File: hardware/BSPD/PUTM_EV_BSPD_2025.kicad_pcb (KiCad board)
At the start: 2 copper layers, 0 parts

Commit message: Layout and connections added
First version of board layout and connections added, to be checked and improved 

I know about 4 DRC errors, I will fix them, but that is what i have for now
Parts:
- added C1: 1u, Capacitor_SMD:C_0805_2012Metric, B.Cu at (137.8, 102.7)
- added C10: 100n, Capacitor_SMD:C_0603_1608Metric, F.Cu at (149.5, 104.2)
- added C11: 100n, Capacitor_SMD:C_0603_1608Metric, F.Cu at (137.7, 93.5)
- added C12: 100n, Capacitor_SMD:C_0603_1608Metric, F.Cu at (149.1, 107.6)
- added C13: 100n, Capacitor_SMD:C_0603_1608Metric, F.Cu at (131.8, 106.6)
- added C14: 100n, Capacitor_SMD:C_0603_1608Metric, B.Cu at (142.7, 103.6)
- added C15: 100n, Capacitor_SMD:C_0603_1608Metric, F.Cu at (139.0, 99.8)
- added C16: 100n, Capacitor_SMD:C_0603_1608Metric, F.Cu at (138.1, 97.4)
- added C17: 100n, Capacitor_SMD:C_0603_1608Metric, F.Cu at (144.9, 97.0)
- added C19: 100n, Capacitor_SMD:C_0603_1608Metric, F.Cu at (147.5, 91.2)
- added C2: 1u, Capacitor_SMD:C_0805_2012Metric, B.Cu at (137.8, 105.7)
- added C20: 100n, Capacitor_SMD:C_0603_1608Metric, F.Cu at (157.4, 99.2)
- added C3: 100nF, Capacitor_SMD:C_0603_1608Metric, B.Cu at (125.9, 94.3)
- added C4: 1u, Capacitor_SMD:C_0805_2012Metric, B.Cu at (137.8, 108.7)
- added C5: 100nF, Capacitor_SMD:C_0603_1608Metric, B.Cu at (125.9, 96.8)
- added C6: 1u, Capacitor_SMD:C_0805_2012Metric, B.Cu at (137.8, 111.7)
- added C7: 1u, Capacitor_SMD:C_0603_1608Metric, F.Cu at (154.7, 92.0)
- added C8: 10n, Capacitor_SMD:C_0603_1608Metric, B.Cu at (147.7, 103.6)
- added C9: 1u, Capacitor_SMD:C_0603_1608Metric, B.Cu at (146.0, 103.6)
- added D1: SK36A-LTP, Diode_SMD:D_SMA, B.Cu at (154.3, 114.4)
- added D2: D5V0L1B2T-7, Diode_SMD:D_SOD-523, F.Cu at (126.3, 107.0)
- added D3: LBD52A24L01, Diode_SMD:D_SOD-523, B.Cu at (126.1, 99.2)
- added D4: D5V0L1B2T-7, Diode_SMD:D_SOD-523, F.Cu at (141.9, 107.6)
- added D5: NSVRB751V40T1G, Diode_SMD:D_SOD-323_HandSoldering, B.Cu at (150.2, 98.6)
- added D8: D5V0L1B2T-7, Diode_SMD:D_SOD-523, F.Cu at (131.7, 103.4)
- added F1: 500mA, Capacitor_SMD:C_1812_4532Metric, B.Cu at (132.1, 112.0)
- added J1: BS1, Connector_Wire:SolderWire-0.1sqmm_1x02_P3.6mm_D0.4mm_OD1mm_Relief, F.Cu at (116.1, 116.0)
- added J2: BS2, Connector_Wire:SolderWire-0.1sqmm_1x02_P3.6mm_D0.4mm_OD1mm_Relief, F.Cu at (116.1, 109.0)
- added J3: BS2, Connector_Wire:SolderWire-0.1sqmm_1x02_P3.6mm_D0.4mm_OD1mm_Relief, F.Cu at (116.1, 102.0)
- added J4: Conn_01x02, Connector_Wire:SolderWire-0.1sqmm_1x02_P3.6mm_D0.4mm_OD1mm_Relief, F.Cu at (116.1, 95.0)
- added JP1: Solder bridge, Jumper:SolderJumper-2_P1.3mm_Open_RoundedPad1.0x1.5mm, F.Cu at (168.1, 107.6)
- added JP2: Solder bridge, Jumper:SolderJumper-2_P1.3mm_Open_RoundedPad1.0x1.5mm, F.Cu at (168.1, 111.4)
- added K2: TE AXICOM IM07DTS, footprints:IM23TS, F.Cu at (162.1, 111.5)
- added Q1: BS170F, Package_TO_SOT_SMD:SOT-23, B.Cu at (159.1, 104.0)
- added R1: 10k, Resistor_SMD:R_0603_1608Metric_Pad0.98x0.95mm_HandSolder, F.Cu at (127.7, 97.2)
- added R10: 10k, Resistor_SMD:R_0603_1608Metric, F.Cu at (148.0, 114.9)
- added R11: 1k, Resistor_SMD:R_0603_1608Metric, F.Cu at (134.4, 107.4)
- added R12: 1k, Resistor_SMD:R_0603_1608Metric, F.Cu at (148.0, 113.2)
- added R13: 10k, Resistor_SMD:R_0603_1608Metric, F.Cu at (136.5, 109.1)
- added R14: 10k, Resistor_SMD:R_0603_1608Metric, F.Cu at (141.9, 110.8)
- added R15: 10k, Resistor_SMD:R_0603_1608Metric, F.Cu at (152.8, 110.0)
- added R18: 50k, Resistor_SMD:R_0603_1608Metric, F.Cu at (154.7, 90.3)
- added R19: 100k, Resistor_SMD:R_0603_1608Metric, F.Cu at (154.7, 93.7)
- added R2: 10k, Resistor_SMD:R_0603_1608Metric_Pad0.98x0.95mm_HandSolder, F.Cu at (127.7, 99.0)
- added R20: 10k, Resistor_SMD:R_0603_1608Metric, F.Cu at (155.7, 104.8)
- added R22: 1k, Resistor_SMD:R_0603_1608Metric, F.Cu at (156.2, 95.5)
- added R23: 1k, Resistor_SMD:R_0603_1608Metric, F.Cu at (156.1, 97.3)
- added R3: 1k, Resistor_SMD:R_0603_1608Metric_Pad0.98x0.95mm_HandSolder, F.Cu at (132.1, 100.2)
- added R4: 10k, Resistor_SMD:R_0603_1608Metric, F.Cu at (158.9, 90.2)
- added R5: 4k, Resistor_SMD:R_0603_1608Metric_Pad0.98x0.95mm_HandSolder, F.Cu at (132.1, 101.8)
- added R6: 10M, Resistor_SMD:R_0603_1608Metric, B.Cu at (144.3, 103.6)
- added R7: 10k, Resistor_SMD:R_0603_1608Metric_Pad0.98x0.95mm_HandSolder, F.Cu at (139.5, 93.3)
- added R8: 10k, Resistor_SMD:R_0603_1608Metric, F.Cu at (126.3, 110.0)
- added R9: 10k, Resistor_SMD:R_0603_1608Metric, F.Cu at (134.4, 105.6)
- added RV1: 20k, Potentiometer_THT:Potentiometer_Bourns_3296W_Vertical, F.Cu at (133.1, 115.1)
- added RV2: 20k, Potentiometer_THT:Potentiometer_Bourns_3296W_Vertical, F.Cu at (143.6, 115.1)
- added RV3: 20k, Potentiometer_THT:Potentiometer_Bourns_3296W_Vertical, F.Cu at (133.7, 92.2)
- added SDC: SDC, Connector_Wire:SolderWire-0.1sqmm_1x02_P3.6mm_D0.4mm_OD1mm_Relief, F.Cu at (169.7, 99.7)
- added TP1: TestPoint, TestPoint:TestPoint_Pad_D1.0mm, B.Cu at (119.3, 112.4)
- added TP10: TestPoint, TestPoint:TestPoint_Pad_D1.0mm, F.Cu at (167.4, 91.6)
- added TP11: TestPoint, TestPoint:TestPoint_Pad_D1.0mm, B.Cu at (145.7, 91.4)
- added TP12: TestPoint, TestPoint:TestPoint_Pad_D1.0mm, F.Cu at (152.8, 104.9)
- added TP13: TestPoint, TestPoint:TestPoint_Pad_D1.0mm, F.Cu at (160.3, 97.3)
- added TP2: TestPoint, TestPoint:TestPoint_Pad_D1.0mm, B.Cu at (119.3, 105.4)
- added TP3: TestPoint, TestPoint:TestPoint_Pad_D1.0mm, B.Cu at (150.2, 91.7)
- added TP4: TestPoint, TestPoint:TestPoint_Pad_D1.0mm, F.Cu at (142.4, 105.0)
- added TP5: TestPoint, TestPoint:TestPoint_Pad_D1.0mm, F.Cu at (145.6, 99.6)
- added TP6: TestPoint, TestPoint:TestPoint_Pad_D1.0mm, F.Cu at (126.6, 102.0)
- added TP7: TestPoint, TestPoint:TestPoint_Pad_D1.0mm, F.Cu at (137.7, 90.6)
- added TP8: TestPoint, TestPoint:TestPoint_Pad_D1.0mm, B.Cu at (119.4, 98.4)
- added TP9: TestPoint, TestPoint:TestPoint_Pad_D1.0mm, B.Cu at (151.0, 94.0)
- added U1: MC78M12CDTG, Package_TO_SOT_SMD:TO-252-3_TabPin2, B.Cu at (133.1, 97.2)
- added U10: LM393B, Package_SO:TSSOP-8_3x3mm_P0.65mm, F.Cu at (160.4, 92.8)
- added U12: 74AHC1G08, Package_TO_SOT_SMD:SC-74A-5_1.55x2.9mm_P0.95mm, F.Cu at (149.1, 96.0)
- added U13: LM393B, Package_SO:TSSOP-8_3x3mm_P0.65mm, F.Cu at (133.2, 97.0)
- added U2: LM1117IMP-5.0, Package_TO_SOT_SMD:SOT-223-3_TabPin2, B.Cu at (130.7, 105.4)
- added U3: 74HC2G14-Q100, Package_SO:TSOP-6_1.65x3.05mm_P0.95mm, F.Cu at (145.0, 91.3)
- added U4: LM393B, Package_SO:TSSOP-8_3x3mm_P0.65mm, F.Cu at (131.2, 110.3)
- added U5: 74AHC1G08, Package_TO_SOT_SMD:SC-74A-5_1.55x2.9mm_P0.95mm, F.Cu at (154.8, 101.8)
- added U6: 74HC2G14-Q100, Package_SO:TSOP-6_1.65x3.05mm_P0.95mm, F.Cu at (139.2, 102.3)
- added U7: LM393B, Package_SO:TSSOP-8_3x3mm_P0.65mm, F.Cu at (147.8, 110.3)
- added U8: NE555DR, Package_SO:SOIC-8_3.9x4.9mm_P1.27mm, B.Cu at (146.2, 97.0)
- added U9: 74HC1G32GV, Package_TO_SOT_SMD:SOT-23-5, F.Cu at (149.0, 101.8)
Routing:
- net +5V: track 0.00 -> 163.9 mm, vias 0 -> 17
- net GND: track 0.00 -> 87.6 mm, vias 0 -> 30
- net +12V: track 0.00 -> 72.1 mm, vias 0 -> 6
- net Net-(D3-A1): track 0.00 -> 44.9 mm, vias 0 -> 2
- net Net-(D5-A): track 0.00 -> 39.1 mm, vias 0 -> 4
- net /Brake Sensors Comparators/Brake1: track 0.00 -> 36.4 mm, vias 0 -> 1
- net /Power Section/LVMS: track 0.00 -> 28.9 mm
- net Net-(D1-A): track 0.00 -> 25.1 mm, vias 0 -> 1
- net /LEM Comparator/LEM_OpAmp_Out: track 0.00 -> 24.7 mm, vias 0 -> 1
- net Net-(J5-Pin_1): track 0.00 -> 24.7 mm, vias 0 -> 1
- net Net-(U8-Q): track 0.00 -> 22.9 mm, vias 0 -> 1
- net Net-(R7-Pad2): track 0.00 -> 21.0 mm
- net Net-(D5-K): track 0.00 -> 18.5 mm, vias 0 -> 2
- net /Brake Sensors Comparators/BrakeLogic: track 0.00 -> 18.4 mm, vias 0 -> 2
- net Net-(J5-Pin_2): track 0.00 -> 17.6 mm, vias 0 -> 1
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- added copper zone on B.Cu, net GND
- added copper zone on F.Cu, net GND
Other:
- board outline added: 58 x 30 mm
- board text added: "24V/LVMS IN"
- board text added: "555 Timer"
- board text added: "BSPD 2025"
- board text added: "Brake Logic"
- board text added: "BrakeSens1"
- board text added: "BrakeSens2"
- board text added: "Current Logic"
- board text added: "CurrentSens"
- board text added: "Designed by:"
- board text added: "IN"
- board text added: "Mikołaj Krzyszkowiak"
- board text added: "OUT"
- board text added: "Power Section"
- board text added: "RC Timer"
- board text added: "Relay Control"
- board text added: "SDC Logic"
- board text added: "{dblquote}It can be a light bulb if you try hard enough!{dblquote}"

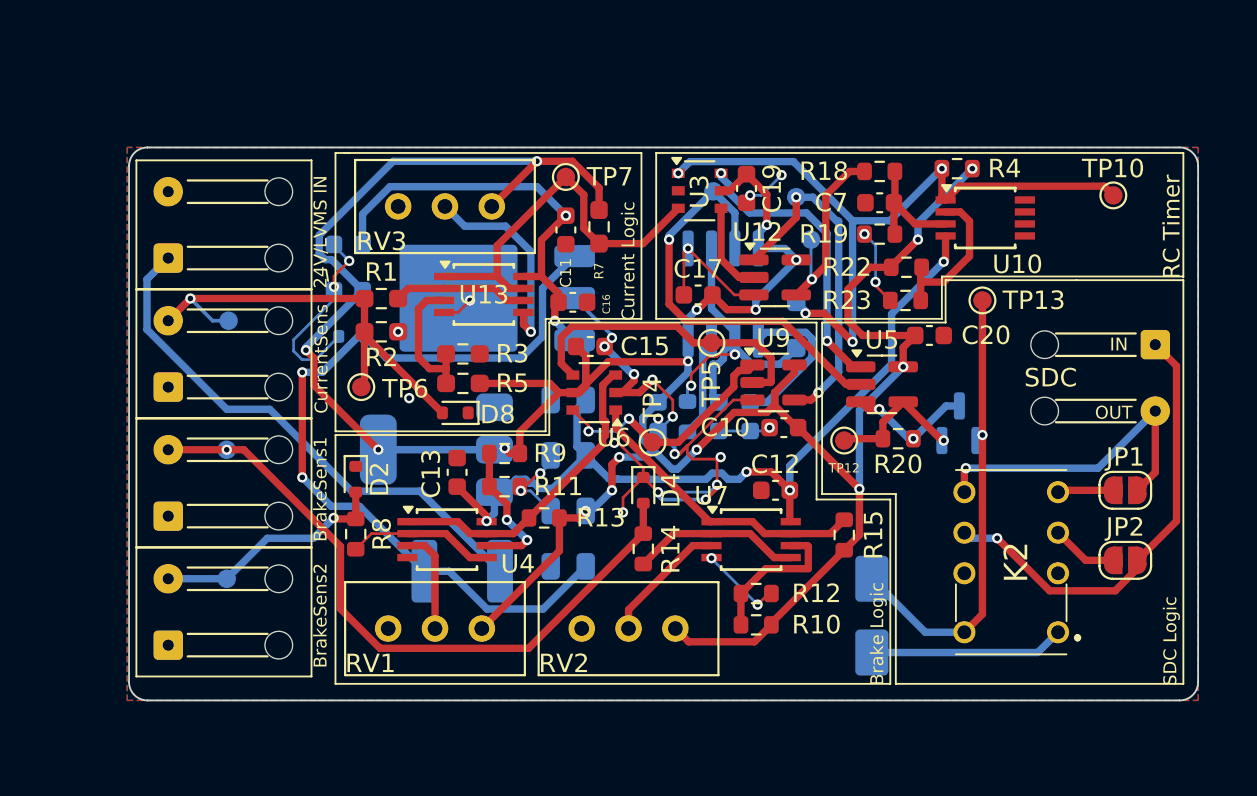
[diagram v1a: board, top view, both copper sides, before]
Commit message: Minor footprint changes + fixed DRC errors
Fixed all critical DRC errors and minor warnings; warnings that were not important/valid have been excluded.

Switched wire holes (in Strain Relief footprint) to 0.4mm from 0.1mm to match 22AWG wire size.
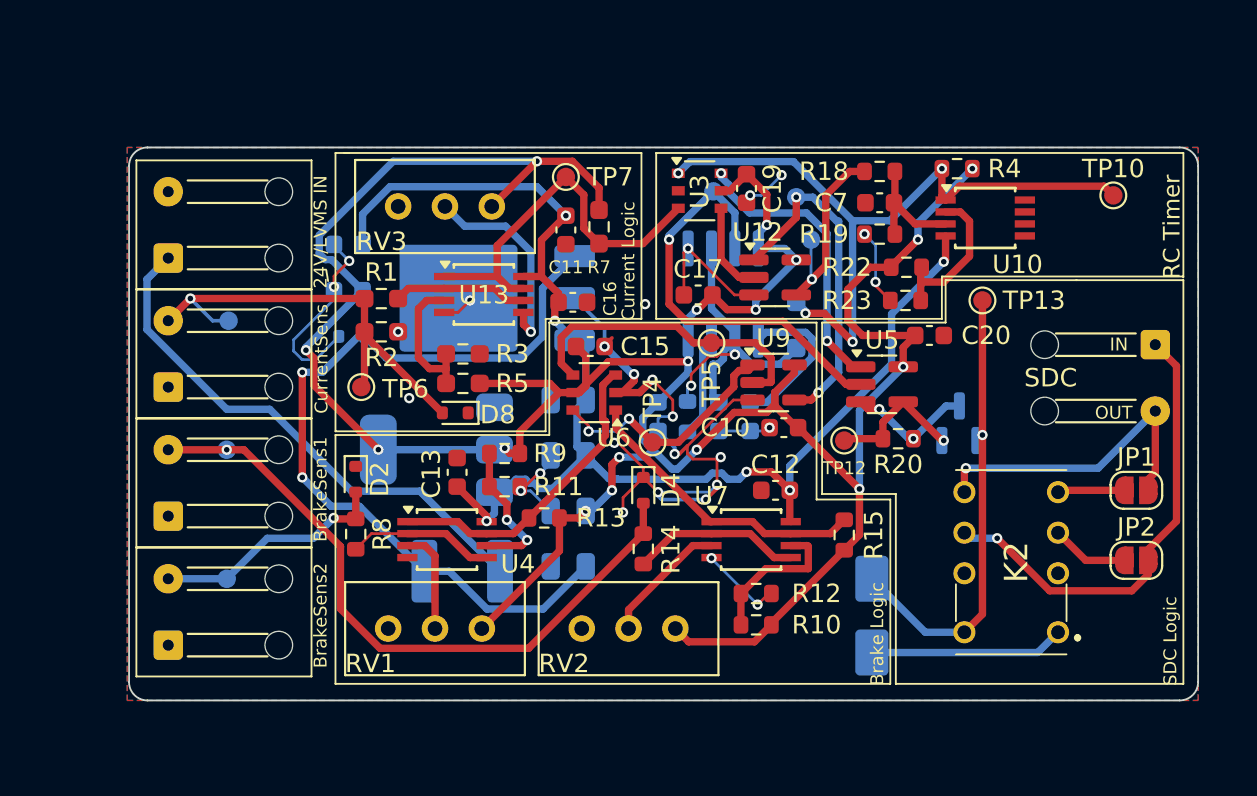
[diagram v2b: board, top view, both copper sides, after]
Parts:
- moved JP1 0.60 mm to (168.7, 107.6)
- moved JP2 0.60 mm to (168.7, 111.4)
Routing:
- net Net-(JP1-A): track 3.04 -> 3.74 mm
- net Net-(J5-Pin_1): track 24.7 -> 25.2 mm
- net GND: vias 30 -> 29
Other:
- board text added: "{dblquote}It can be a light bulb!{dblquote}"
- board text removed: "{dblquote}It can be a light bulb if you try hard enough!{dblquote}"

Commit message: Major changes. Read ext. description.
- Changed board to 4 layers due to trace fitment issues (or skill issues)
- Added mounting holes to be compatible with previous gen. of board
- Added unassigned footprints
- Fully fixed DRC errors
- Fixed comp. issues with schematic
- Added missing custom footprints to library (and made the library)
NOTE: Ignore "not matching with library copy" - It's matching. Trust me.
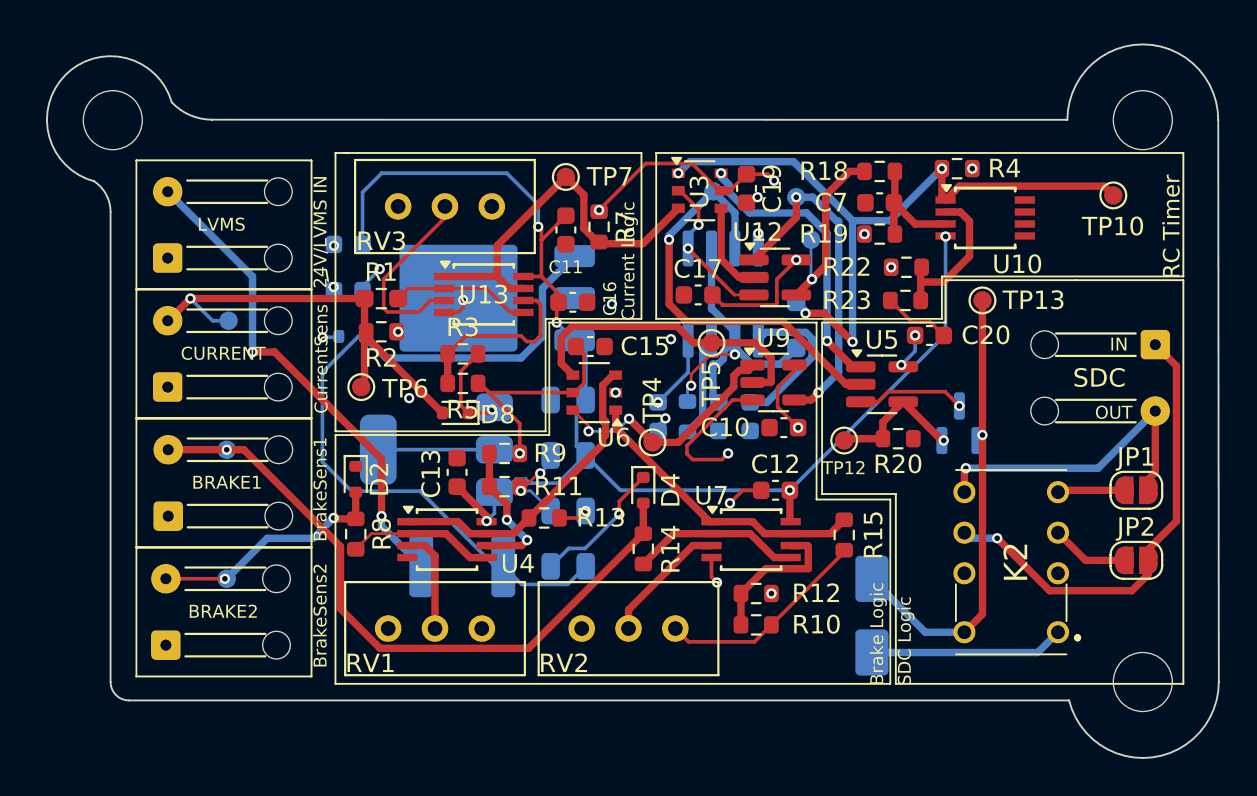
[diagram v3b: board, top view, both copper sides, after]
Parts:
- removed F1: 500mA, Capacitor_SMD:C_1812_4532Metric
- added 500mA/30V1: 500mA, Diode_SMD:D_1812_4532Metric_Pad1.30x3.40mm_HandSolder, B.Cu at (132.1, 111.7)
- added H1: MountingHole, MountingHole:MountingHole_3.2mm_M3_ISO7380, F.Cu at (113.1, 87.5)
- added H3: MountingHole, MountingHole:MountingHole_3.2mm_M3_ISO7380, F.Cu at (169.0, 87.5)
- added H4: MountingHole, MountingHole:MountingHole_3.2mm_M3_ISO7380, F.Cu at (169.0, 118.0)
- J1, J2, J3, J4: footprint Connector_Wire:SolderWire-0.1sqmm_1x02_P3.6mm_D0.4mm_OD1mm_Relief -> footprints:Wire_StrainRelief
- J5: renamed from SDC; footprint Connector_Wire:SolderWire-0.1sqmm_1x02_P3.6mm_D0.4mm_OD1mm_Relief -> footprints:Wire_StrainRelief
- R2, R3, R5, R7: footprint Resistor_SMD:R_0603_1608Metric_Pad0.98x0.95mm_HandSolder -> Resistor_SMD:R_0603_1608Metric
- moved J2 3.63 mm to (119.3, 107.2)
- moved J5 3.63 mm to (166.5, 101.5)
- moved J3 3.61 mm to (119.2, 100.2)
- moved J4 3.61 mm to (119.2, 93.2)
- moved J1 3.52 mm to (119.2, 114.2)
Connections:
- J4 pad 1: /Power Section/LVMS -> GND
- J4 pad 2: GND -> /Power Section/LVMS
- R3 pad 1: Net-(U13A-+) -> Net-(U13B--)
- R5 pad 2: Net-(U13A-+) -> Net-(U13B--)
- RV3 pad 2: Net-(U13B-+) -> Net-(U13A-+)
- U13 pad 5: Net-(U13B-+) -> Net-(U13A--)
- U13 pad 6: Net-(U13A--) -> Net-(U13B--)
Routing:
- net +5V: track 163.9 -> 71.3 mm, vias 17 -> 13
- net GND: track 87.6 -> 55.1 mm, vias 29 -> 23
- net Net-(U13B-+): track 11.2 -> 0.00 mm, vias 1 -> 0
- net Net-(U13B--): track 0.00 -> 10.0 mm
- net Net-(D3-A1): track 44.9 -> 41.1 mm, vias 2 -> 0
- net Net-(U13A-+): track 7.58 -> 10.5 mm
- net /Power Section/LVMS: track 28.9 -> 26.5 mm, vias 0 -> 2
- net +12V: track 72.1 -> 72.7 mm, vias 6 -> 5
- net /Brake Sensors Comparators/Brake2: track 13.0 -> 12.5 mm, vias 1 -> 2
- removed copper zone on B.Cu, net GND
- removed copper zone on F.Cu, net GND
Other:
- board size 58 x 30 mm -> 63.6 x 38.7 mm
- copper layers 2 -> 4
- board text added: "BRAKE1"
- board text added: "BRAKE2"
- board text added: "CURRENT"
- board text added: "LVMS"
- board text added: "SDC"

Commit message: Fixed relay routing + changed board shape
Board shape changed to accomodate M3 mounting holes, matching older BSPD's.
Fixed an issue where the relay coil was no connected to LVMS due to skill issues in hierarhical sheeting.
LVMS (+24VDC) line breakaway placed behind the fuse.
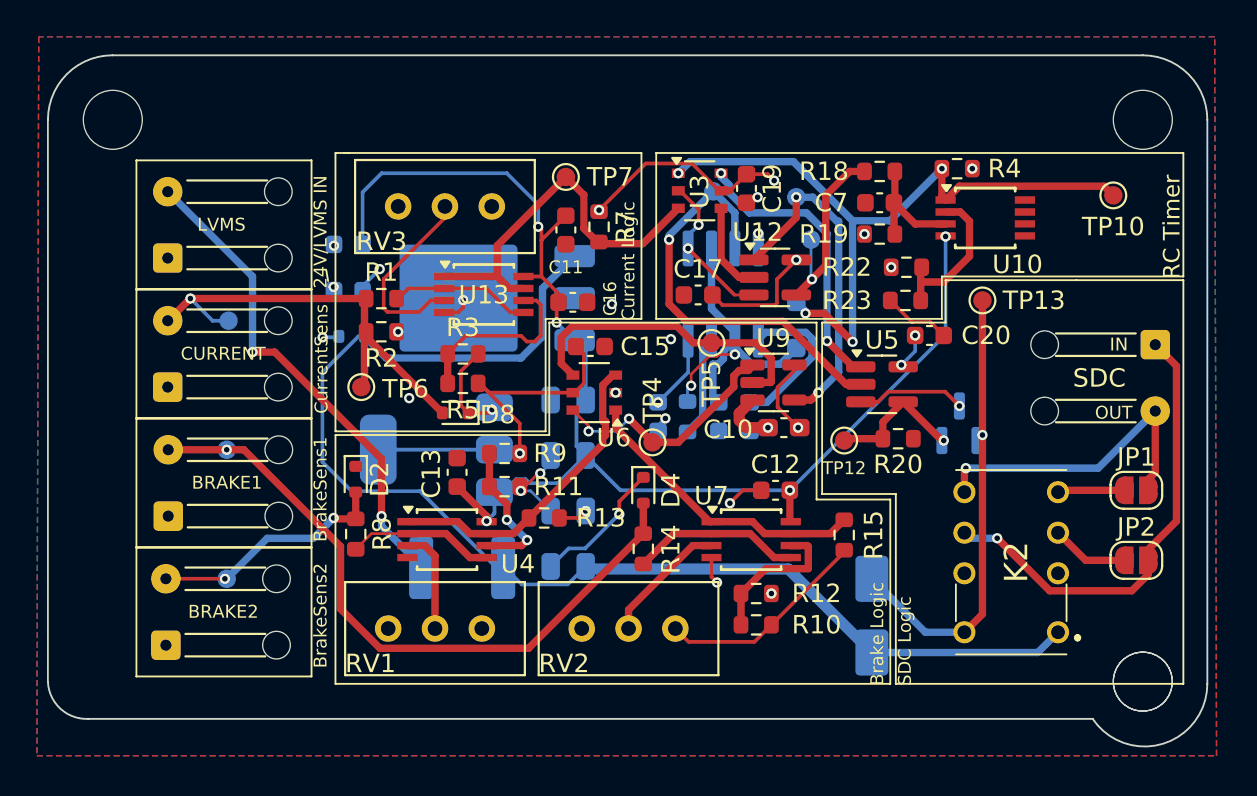
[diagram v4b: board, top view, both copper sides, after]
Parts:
- added ?: , , F.Cu at (169.0, 118.0)
- C10: footprint Capacitor_SMD:C_0603_1608Metric -> Capacitor_SMD:C_0603_1608Metric_Pad1.08x0.95mm_HandSolder
- R1: footprint Resistor_SMD:R_0603_1608Metric_Pad0.98x0.95mm_HandSolder -> Resistor_SMD:R_0603_1608Metric
- moved 500mA/30V1 0.10 mm to (132.1, 111.8)
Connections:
- net /Power Section/LVMS renamed Net-(J4-Pin_2)
- 500mA/30V1 pad 2: Net-(D3-A1) -> /LVMS_Coil
- C6 pad 1: Net-(D3-A1) -> /LVMS_Coil
- D1 pad 1: /LVMS -> /LVMS_Coil
- D3 pad 1: Net-(D3-A1) -> /LVMS_Coil
- K2 pad 1: /LVMS -> /LVMS_Coil
- U1 pad 1: Net-(D3-A1) -> /LVMS_Coil
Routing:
- net /LVMS_Coil: track 0.00 -> 69.1 mm
- net Net-(D3-A1): track 41.1 -> 0.00 mm
- net /LVMS: track 10.6 -> 0.00 mm
- net GND: track 55.1 -> 50.7 mm
- added copper zone on In2.Cu, net +5V
- added copper zone on B.Cu, net GND
- added copper zone on F.Cu, net GND
- added copper zone on In1.Cu, net GND
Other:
- board size 63.6 x 38.7 mm -> 62.9 x 37.5 mm

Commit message: Minor changes. Read ext. description for info.
Removed isolated copper (ground) islands on both layers
Changed timing capacitors values to compensate DC Bias (+0.5uF)
Changed board shape 
Relocated TVS Diodes to be directly connected with inputs
Fixed relay wiring issues
Added space for additional capacitors to compensate DC Bias if needed
Fixed overlapped part references
Added mounting holes, and relocated a connector to accomodate screw head.
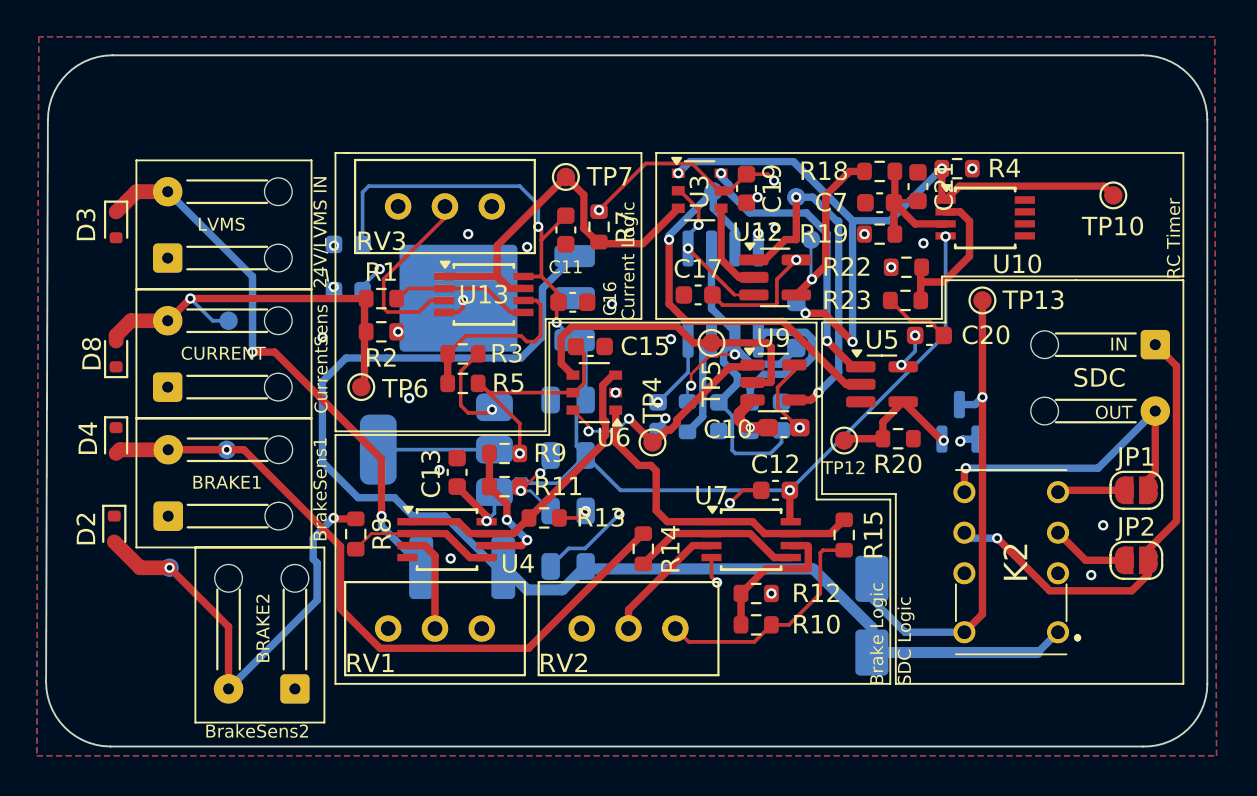
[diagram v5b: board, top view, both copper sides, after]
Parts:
- removed ?: , 
- removed H1, H3, H4: MountingHole, MountingHole:MountingHole_3.2mm_M3_ISO7380
- added C18: -, Capacitor_SMD:C_0603_1608Metric, B.Cu at (149.4, 103.6)
- added C21: -, Capacitor_SMD:C_0603_1608Metric, F.Cu at (156.8, 91.1)
- C7, C9: value 1u -> 1u5
- D3: moved to F.Cu
- moved D4 28.7 mm to (113.3, 104.9)
- moved D8 18.7 mm to (113.3, 100.2), turned to 90 degrees
- moved D3 14.1 mm to (113.3, 93.2), turned to -90 degrees
- moved D2 13.4 mm to (113.2, 109.7)
- moved TP1 3.16 mm to (116.2, 111.8)
- moved J1 2.29 mm to (121.2, 115.2), turned to 180 degrees
- moved Q1 0.08 mm to (159.1, 103.9)
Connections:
- D3 pad 1: /LVMS_Coil -> Net-(J4-Pin_2)
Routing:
- net /Brake Sensors Comparators/Brake2: track 12.5 -> 24.5 mm
- net GND: track 50.7 -> 42.3 mm, vias 23 -> 31
- net Net-(D5-K): track 18.5 -> 25.3 mm
- net Net-(J4-Pin_2): track 26.5 -> 29.7 mm
- net /LEM Comparator/LEM_OpAmp_Out: track 24.7 -> 22.2 mm
- net Net-(R15-Pad2): track 16.0 -> 17.8 mm
- net +5V: track 71.3 -> 73.0 mm
- net Net-(D1-A): track 25.1 -> 26.7 mm
- net Net-(U10A-+): track 6.72 -> 8.06 mm
- net /Brake Sensors Comparators/Brake1: track 36.4 -> 37.7 mm
- net /Brake Sensors Comparators/BrakeLogic: track 18.4 -> 19.1 mm
- net +12V: track 72.7 -> 72.1 mm
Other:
- board size 62.9 x 37.5 mm -> 63 x 37.5 mm
